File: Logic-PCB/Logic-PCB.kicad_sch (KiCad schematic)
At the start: 144 parts, among them IC1 74LVC1G74DC-Q100H, IC10 74AUP1G32GW-Q100H, IC11 TMUX1208QRSVRQ1, IC12 TMUX1208QRSVRQ1, IC13 TMUX1208QRSVRQ1, IC14 TMUX1208QRSVRQ1, IC15 TMUX1208QRSVRQ1, IC16 TMUX1208QRSVRQ1, IC17 TMUX1208QRSVRQ1, IC18 TMUX1208QRSVRQ1, IC19 TMUX1208QRSVRQ1, IC2 74HC73D,653, IC20 TLC555QDRQ1, IC21 74AUP1T87GWH, IC3 SN74LVC1G02DBVR, IC4 SN74LVC1G02DBVR, IC5 NCV4274CDT33RKG, IC6 74HC73D,653, IC7 74HC73D,653, IC8 SN74LVC1G11MDCKREP, IC9 SN74LVC1G11MDCKREP, Q1 BC847,215, Q10 PMV100EPAR, Q11 2N7002_HAMR, Q12 2N7002_HAMR, Q13 BC858B,235, Q2 BC847,215, Q3 BC847,215, Q4 BC847,215, Q5 PMV100EPAR, Q6 PMV100EPAR, Q7 2N7002_HAMR, Q8 2N7002_HAMR, Q9 PMV100EPAR, SW1 SW_Push, SW2 SW_Push, U1 BAT-HLD-001-TR, U2 NC7S08M5X, U3 74AHC1G86W5-7

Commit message: Comment out diode
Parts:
- U2: footprint (none) -> Connector:USB-C UJC-HP-G-5-SMT-TR
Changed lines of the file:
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@@
       (effects (font (size 1.27 1.27)))
     )
-    (property "Footprint" "" (at 143.256 81.28 0)
+    (property "Footprint" "Connector:USB-C UJC-HP-G-5-SMT-TR" (at 143.256 81.28 0)
       (effects (font (size 1.27 1.27)) hide)
     )
@@
       (project "Logic-PCB"
         (path "/eaab10dc-c7f1-4dfd-85a3-a6211aca9d04"
-          (reference "D10") (unit 1)
-        )
-      )
+          (reference "#D10") (unit 1)
+        )
+      )

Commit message: update
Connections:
- net 3V before switch: now also C5.1, C7.1, IC5.3 (OUTPUT); no longer D6.1
- new net #3V before switch: D6.1
- now unconnected: D6.2
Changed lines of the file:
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@@
     )
   )
-  (global_label "3V before switch" (shape input) (at 131.572 115.316 180) (fields_autoplaced)
+  (global_label "#3V before switch" (shape input) (at 131.572 114.1476 180) (fields_autoplaced)
     (effects (font (size 1.27 1.27)) (justify right))
-    (property "Intersheetrefs" "${INTERSHEET_REFS}" (at 112.5191 115.316 0)
+    (property "Intersheetrefs" "${INTERSHEET_REFS}" (at 111.2491 114.1476 0)
       (effects (font (size 1.27 1.27)) (justify right) hide)
     )
@@
     )
   )
+  (global_label "3V before switch" (shape input) (at 131.572 130.556 180) (fields_autoplaced)
+    (effects (font (size 1.27 1.27)) (justify right))
+    (property "Intersheetrefs" "${INTERSHEET_REFS}" (at 112.5191 130.556 0)
+      (effects (font (size 1.27 1.27)) (justify right) hide)
+    )
+  )
   (global_label "Button B" (shape input) (at 82.042 216.154 180) (fields_autoplaced)
     (effects (font (size 1.27 1.27)) (justify right))
@@
     )
   )
+  (symbol (lib_id "SamacSys_Parts:LSM115JE3_TR13") (at 131.572 111.6076 270) (unit 1)
+    (in_bom yes) (on_board yes) (dnp no)
+    (property "Reference" "D6" (at 112.522 121.7676 90)
+      (effects (font (size 1.27 1.27)) (justify left))
+    )
+    (property "Value" "LSM115JE3_TR13" (at 112.522 124.3076 90)
+      (effects (font (size 1.27 1.27)) (justify left))
+    )
+    (property "Footprint" "SamacSys_Parts:DIOM5436X330N" (at 135.382 124.3076 0)
+      (effects (font (size 1.27 1.27)) (justify left) hide)
+    )
+    (property "Datasheet" "https://media.digikey.com/pdf/Data%20Sheets/Microsemi%20PDFs/LSM115J.pdf" (at 132.842 124.3076 0)
+      (effects (font (size 1.27 1.27)) (justify left) hide)
+    )
+    (property "Description" "Schottky Diodes & Rectifiers Schottky" (at 130.302 124.3076 0)
+      (effects (font (size 1.27 1.27)) (justify left) hide)
+    )
+    (property "Height" "3.3" (at 127.762 124.3076 0)
+      (effects (font (size 1.27 1.27)) (justify left) hide)
+    )
+    (property "Manufacturer_Name" "Microsemi Corporation" (at 125.222 124.3076 0)
+      (effects (font (size 1.27 1.27)) (justify left) hide)
+    )
+    (property "Manufacturer_Part_Number" "LSM115JE3/TR13" (at 122.682 124.3076 0)
+      (effects (font (size 1.27 1.27)) (justify left) hide)
+    )
+    (property "Mouser Part Number" "494-LSM115JE3/TR13" (at 120.142 124.3076 0)
+      (effects (font (size 1.27 1.27)) (justify left) hide)
+    )
+    (property "Mouser Price/Stock" "https://www.mouser.co.uk/ProductDetail/Microchip-Microsemi/LSM115JE3-TR13/?qs=6jAvgNDGUA8H9k1qUsKdHA%3D%3D" (at 117.602 124.3076 0)
+      (effects (font (size 1.27 1.27)) (justify left) hide)
+    )
+    (property "Arrow Part Number" "LSM115JE3/TR13" (at 115.062 124.3076 0)
+      (effects (font (size 1.27 1.27)) (justify left) hide)
+    )
+    (property "Arrow Price/Stock" "https://www.arrow.com/en/products/lsm115je3tr13/microsemi" (at 112.522 124.3076 0)
+      (effects (font (size 1.27 1.27)) (justify left) hide)
+    )
+    (pin "1")
+    (pin "2")
+    (instances
+      (project "Logi-PCB-2"
+        (path "/4826693f-0a14-47f3-8ca1-fd74785177a0"
+          (reference "D6") (unit 1)
+        )
+      )
+      (project "Logic-PCB"
+        (path "/eaab10dc-c7f1-4dfd-85a3-a6211aca9d04"
+          (reference "#D10") (unit 1)
+        )
+      )
+    )
+  )
   (symbol (lib_id "Device:C") (at 383.032 154.686 0) (unit 1)
     (in_bom yes) (on_board yes) (dnp no)
@@
         )
       )
-    )
-  )
-  (symbol (lib_id "SamacSys_Parts:LSM115JE3_TR13") (at 131.572 112.776 270) (unit 1)
-    (in_bom yes) (on_board yes) (dnp no)
-    (property "Reference" "D6" (at 112.522 122.936 90)
-      (effects (font (size 1.27 1.27)) (justify left))
-    )
-    (property "Value" "LSM115JE3_TR13" (at 112.522 125.476 90)
-      (effects (font (size 1.27 1.27)) (justify left))
-    )
-    (property "Footprint" "SamacSys_Parts:DIOM5436X330N" (at 135.382 125.476 0)
-      (effects (font (size 1.27 1.27)) (justify left) hide)
-    )
-    (property "Datasheet" "https://media.digikey.com/pdf/Data%20Sheets/Microsemi%20PDFs/LSM115J.pdf" (at 132.842 125.476 0)
-      (effects (font (size 1.27 1.27)) (justify left) hide)
-    )
-    (property "Description" "Schottky Diodes & Rectifiers Schottky" (at 130.302 125.476 0)
-      (effects (font (size 1.27 1.27)) (justify left) hide)
-    )
-    (property "Height" "3.3" (at 127.762 125.476 0)
-      (effects (font (size 1.27 1.27)) (justify left) hide)
-    )
-    (property "Manufacturer_Name" "Microsemi Corporation" (at 125.222 125.476 0)
-      (effects (font (size 1.27 1.27)) (justify left) hide)
-    )
-    (property "Manufacturer_Part_Number" "LSM115JE3/TR13" (at 122.682 125.476 0)
-      (effects (font (size 1.27 1.27)) (justify left) hide)
-    )
-    (property "Mouser Part Number" "494-LSM115JE3/TR13" (at 120.142 125.476 0)
-      (effects (font (size 1.27 1.27)) (justify left) hide)
-    )
-    (property "Mouser Price/Stock" "https://www.mouser.co.uk/ProductDetail/Microchip-Microsemi/LSM115JE3-TR13/?qs=6jAvgNDGUA8H9k1qUsKdHA%3D%3D" (at 117.602 125.476 0)
-      (effects (font (size 1.27 1.27)) (justify left) hide)
-    )
-    (property "Arrow Part Number" "LSM115JE3/TR13" (at 115.062 125.476 0)
-      (effects (font (size 1.27 1.27)) (justify left) hide)
-    )
-    (property "Arrow Price/Stock" "https://www.arrow.com/en/products/lsm115je3tr13/microsemi" (at 112.522 125.476 0)
-      (effects (font (size 1.27 1.27)) (justify left) hide)
-    )
-    (pin "1")
-    (pin "2")
-    (instances
-      (project "Logi-PCB-2"
-        (path "/4826693f-0a14-47f3-8ca1-fd74785177a0"
-          (reference "D6") (unit 1)
-        )
-      )
-      (project "Logic-PCB"
-        (path "/eaab10dc-c7f1-4dfd-85a3-a6211aca9d04"
-          (reference "#D10") (unit 1)
-        )
-      )

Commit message: bumps
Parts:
- C6: value 100n -> .1u
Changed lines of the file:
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@@
   (symbol (lib_id "Device:C") (at 144.272 119.126 0) (unit 1)
     (in_bom yes) (on_board yes) (dnp no) (fields_autoplaced)
-    (property "Reference" "C6" (at 148.082 117.856 0)
+    (property "Reference" "C6" (at 147.32 117.856 0)
       (effects (font (size 1.27 1.27)) (justify left))
     )
-    (property "Value" "100n" (at 148.082 120.396 0)
+    (property "Value" ".1u" (at 147.32 120.396 0)
       (effects (font (size 1.27 1.27)) (justify left))
     )

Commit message: Final
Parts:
- added D7: LED, LED_SMD:LED_0402_1005Metric, symbol Device:LED
- added R9: 100, Resistor_SMD:R_0402_1005Metric, symbol Device:R
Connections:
- net GND: now also D7.1 (K)
- net at IC6.13 (1~{Q}): now also R9.2
- new net: D7.2 (A), R9.1
- no-connect marks 19 -> 18
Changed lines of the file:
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@@
   (no_connect (at 165.862 168.656))
   (no_connect (at 74.422 97.536))
-  (no_connect (at 313.182 96.266))
   (no_connect (at 132.842 168.656))
   (no_connect (at 285.242 103.886))
@@
     (stroke (width 0) (type default))
   )
+  (wire (pts (xy 324.8914 95.8342) (xy 324.8914 96.266))
+    (stroke (width 0) (type default))
+  )
   (wire (pts (xy 212.852 72.136) (xy 221.742 72.136))
     (stroke (width 0) (type default))
@@
     (stroke (width 0) (type default))
   )
+  (wire (pts (xy 313.182 96.266) (xy 324.8914 96.266))
+    (stroke (width 0) (type default))
+  )
   (wire (pts (xy 230.632 36.576) (xy 235.712 36.576))
     (stroke (width 0) (type default))
@@
     )
   )
+  (symbol (lib_id "Device:R") (at 324.8914 92.0242 0) (unit 1)
+    (in_bom yes) (on_board yes) (dnp no) (fields_autoplaced)
+    (property "Reference" "R9" (at 322.3514 93.2942 0)
+      (effects (font (size 1.27 1.27)) (justify right))
+    )
+    (property "Value" "100" (at 322.3514 90.7542 0)
+      (effects (font (size 1.27 1.27)) (justify right))
+    )
+    (property "Footprint" "Resistor_SMD:R_0402_1005Metric" (at 323.1134 92.0242 90)
+      (effects (font (size 1.27 1.27)) hide)
+    )
+    (property "Datasheet" "~" (at 324.8914 92.0242 0)
+      (effects (font (size 1.27 1.27)) hide)
+    )
+    (pin "1")
+    (pin "2")
+    (instances
+      (project "Logi-PCB-2"
+        (path "/4826693f-0a14-47f3-8ca1-fd74785177a0"
+          (reference "R9") (unit 1)
+        )
+      )
+      (project "Logic-PCB"
+        (path "/da0a227d-8c5e-40bd-9f97-ddcba2042b7f"
+          (reference "R1") (unit 1)
+        )
+      )
+      (project "Logic-PCB"
+        (path "/eaab10dc-c7f1-4dfd-85a3-a6211aca9d04"
+          (reference "R33") (unit 1)
+        )
+      )
+    )
+  )
   (symbol (lib_id "Device:R") (at 118.11 69.85 180) (unit 1)
     (in_bom yes) (on_board yes) (dnp no) (fields_autoplaced)
@@
       (project "Logic-PCB"
         (path "/eaab10dc-c7f1-4dfd-85a3-a6211aca9d04"
-          (reference "R34") (unit 1)
+          (reference "#R34") (unit 1)
         )
       )
@@
       (project "Logic-PCB"
         (path "/eaab10dc-c7f1-4dfd-85a3-a6211aca9d04"
-          (reference "D20") (unit 1)
+          (reference "#D20") (unit 1)
         )
       )
@@
       (project "Logic-PCB"
         (path "/eaab10dc-c7f1-4dfd-85a3-a6211aca9d04"
-          (reference "R33") (unit 1)
+          (reference "#R33") (unit 1)
         )
       )
@@
     )
   )
+  (symbol (lib_id "power:GND") (at 324.8914 80.5942 180) (unit 1)
+    (in_bom yes) (on_board yes) (dnp no) (fields_autoplaced)
+    (property "Reference" "#PWR046" (at 324.8914 74.2442 0)
+      (effects (font (size 1.27 1.27)) hide)
+    )
+    (property "Value" "GND" (at 324.8914 75.5142 0)
+      (effects (font (size 1.27 1.27)))
+    )
+    (property "Footprint" "" (at 324.8914 80.5942 0)
+      (effects (font (size 1.27 1.27)) hide)
+    )
+    (property "Datasheet" "" (at 324.8914 80.5942 0)
+      (effects (font (size 1.27 1.27)) hide)
+    )
+    (pin "1")
+    (instances
+      (project "Logi-PCB-2"
+        (path "/4826693f-0a14-47f3-8ca1-fd74785177a0"
+          (reference "#PWR046") (unit 1)
+        )
+      )
+      (project "Logic-PCB"
+        (path "/da0a227d-8c5e-40bd-9f97-ddcba2042b7f"
+          (reference "#PWR02") (unit 1)
+        )
+      )
+      (project "Logic-PCB"
+        (path "/eaab10dc-c7f1-4dfd-85a3-a6211aca9d04"
+          (reference "#PWR030") (unit 1)
+        )
+      )
+    )
+  )
   (symbol (lib_id "power:GND") (at 404.622 50.546 0) (unit 1)
     (in_bom yes) (on_board yes) (dnp no) (fields_autoplaced)
@@
       (project "Logic-PCB"
         (path "/eaab10dc-c7f1-4dfd-85a3-a6211aca9d04"
-          (reference "D16") (unit 1)
+          (reference "#D16") (unit 1)
         )
       )
@@
     )
   )
+  (symbol (lib_id "Device:LED") (at 324.8914 84.4042 270) (unit 1)
+    (in_bom yes) (on_board yes) (dnp no) (fields_autoplaced)
+    (property "Reference" "D7" (at 321.0814 84.0867 90)
+      (effects (font (size 1.27 1.27)) (justify right))
+    )
+    (property "Value" "LED" (at 321.0814 81.5467 90)
+      (effects (font (size 1.27 1.27)) (justify right))
+    )
+    (property "Footprint" "LED_SMD:LED_0402_1005Metric" (at 324.8914 84.4042 0)
+      (effects (font (size 1.27 1.27)) hide)
+    )
+    (property "Datasheet" "~" (at 324.8914 84.4042 0)
+      (effects (font (size 1.27 1.27)) hide)
+    )
+    (pin "1")
+    (pin "2")
+    (instances
+      (project "Logi-PCB-2"
+        (path "/4826693f-0a14-47f3-8ca1-fd74785177a0"
+          (reference "D7") (unit 1)
+        )
+      )
+      (project "Logic-PCB"
+        (path "/da0a227d-8c5e-40bd-9f97-ddcba2042b7f"
+          (reference "D1") (unit 1)
+        )
+      )
+      (project "Logic-PCB"
+        (path "/eaab10dc-c7f1-4dfd-85a3-a6211aca9d04"
+          (reference "D10") (unit 1)
+        )
+      )
+    )
+  )
   (symbol (lib_id "Device:LED") (at 404.622 46.736 90) (unit 1)
     (in_bom yes) (on_board yes) (dnp no) (fields_autoplaced)
@@
       (project "Logic-PCB"
         (path "/eaab10dc-c7f1-4dfd-85a3-a6211aca9d04"
-          (reference "D19") (unit 1)
+          (reference "#D19") (unit 1)
         )
       )
@@
       (project "Logic-PCB"
         (path "/eaab10dc-c7f1-4dfd-85a3-a6211aca9d04"
-          (reference "D17") (unit 1)
+          (reference "#D17") (unit 1)
         )
       )
@@
       (project "Logic-PCB"
         (path "/eaab10dc-c7f1-4dfd-85a3-a6211aca9d04"
-          (reference "R37") (unit 1)
+          (reference "#R37") (unit 1)
         )
       )
@@
       (project "Logic-PCB"
         (path "/eaab10dc-c7f1-4dfd-85a3-a6211aca9d04"
-          (reference "R36") (unit 1)
+          (reference "#R36") (unit 1)
         )
       )

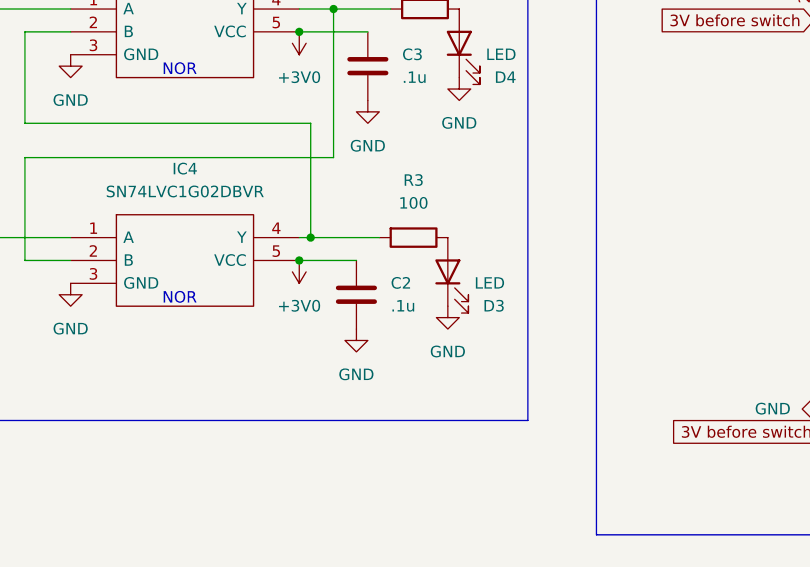
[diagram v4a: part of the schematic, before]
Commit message: Cap fix
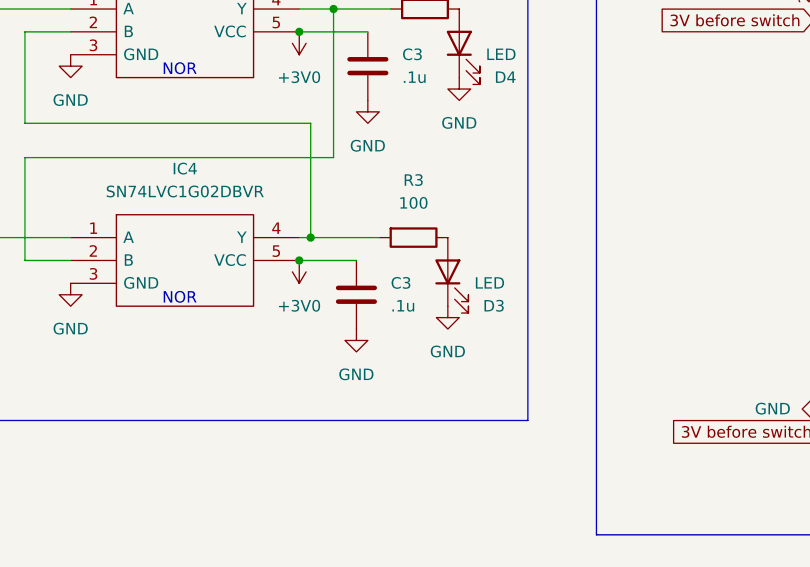
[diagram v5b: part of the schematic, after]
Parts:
- removed C2: .1u, Capacitor_SMD:C_01005_0402Metric, symbol Device:C
- added C3: .1u, Capacitor_SMD:C_0402_1005Metric, symbol Device:C
- C1, C10, C11, C12, C13, C14, C15, C16, C17, C18, C19, C20, C21, C22, C23, C24, C25, C26, C27, C28, C29, C3, C30, C31, C4, C5, C6, C7, C8, C9: footprint Capacitor_SMD:C_01005_0402Metric -> Capacitor_SMD:C_0402_1005Metric
- IC10, IC21: footprint SOT65P212X110-5N -> SamacSys_Parts:SOT65P212X110-5N
- IC5: footprint NCV4274CDT33RKG -> SamacSys_Parts:NCV4274CDT33RKG
- Q1, Q2, Q3, Q4: footprint BC847215 -> SamacSys_Parts:BC847215
- Q10, Q5, Q6, Q9: footprint SOT95P230X110-3N -> SamacSys_Parts:SOT95P230X110-3N
- Q11, Q12, Q7, Q8: footprint 2N7002HAMR -> SamacSys_Parts:2N7002HAMR
- Q13: footprint BC858B235 -> SamacSys_Parts:BC858B235
- U2: footprint SOT95P280X145-5N -> SamacSys_Parts:SOT95P280X145-5N
- U3: footprint SOT95P285X130-5N -> SamacSys_Parts:SOT95P285X130-5N
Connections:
- net +3V0: now also C3.1
- net GND: now also C3.2

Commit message: sch. switch update
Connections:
- net #3V before switch: now also S1.4 (NO_1)
- net 3V before switch: no longer S1.4 (NO_1)
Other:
- note added: "#On/Off Switch"
- note removed: "On/Off Switch"
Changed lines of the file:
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@@
     (effects (font (size 1.27 1.27)) (justify left bottom))
   )
-  (text "On/Off Switch" (at 141.732 158.496 0)
+  (text "#On/Off Switch" (at 141.732 158.496 0)
     (effects (font (size 1.27 1.27)) (justify left bottom))
   )
@@
     )
   )
-  (global_label "3V before switch" (shape input) (at 132.842 176.276 180) (fields_autoplaced)
-    (effects (font (size 1.27 1.27)) (justify right))
-    (property "Intersheetrefs" "${INTERSHEET_REFS}" (at 113.7891 176.276 0)
-      (effects (font (size 1.27 1.27)) (justify right) hide)
-    )
+  (global_label "#3V before switch" (shape input) (at 132.842 176.276 180) (fields_autoplaced)
+    (effects (font (size 1.27 1.27)) (justify right))
+    (property "Intersheetrefs" "${INTERSHEET_REFS}" (at 112.5191 176.276 0)
+      (effects (font (size 1.27 1.27)) (justify right) hide)
+    )

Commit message: Pictures
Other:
- note added: "On/Off Switch"
- note removed: "#On/Off Switch"
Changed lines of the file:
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@@
     (stroke (width 0) (type default))
   )
-  (rectangle (start 16.764 196.088) (end 178.054 347.726)
+  (rectangle (start 16.764 196.088) (end 183.134 347.726)
     (stroke (width 0) (type default))
     (fill (type none))
   )
-  (rectangle (start 17.272 17.526) (end 99.822 175.006)
+  (rectangle (start 17.272 17.526) (end 104.394 175.006)
     (stroke (width 0) (type default))
     (fill (type none))
@@
     (effects (font (size 1.27 1.27)) (justify left bottom))
   )
-  (text "USB-C Connector" (at 140.462 51.816 0)
+  (text "USB-C Connector" (at 134.874 54.102 0)
     (effects (font (size 1.27 1.27)) (justify left bottom))
   )
-  (text "#On/Off Switch" (at 141.732 158.496 0)
+  (text "On/Off Switch" (at 141.732 158.496 0)
     (effects (font (size 1.27 1.27)) (justify left bottom))
   )
@@
   )
   (symbol (lib_id "power:+3V0") (at 333.502 117.856 90) (unit 1)
-    (in_bom yes) (on_board yes) (dnp no) (fields_autoplaced)
+    (in_bom yes) (on_board yes) (dnp no)
     (property "Reference" "#PWR051" (at 337.312 117.856 0)
       (effects (font (size 1.27 1.27)) hide)
     )
-    (property "Value" "+3V0" (at 329.692 117.856 90)
+    (property "Value" "+3V0" (at 333.756 115.57 90)
       (effects (font (size 1.27 1.27)) (justify left))
     )

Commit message: Cleaned up CMOS
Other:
- note added: "#On/Off Switch"
- note removed: "On/Off Switch"
- moved on the sheet: R33, R41, R42
